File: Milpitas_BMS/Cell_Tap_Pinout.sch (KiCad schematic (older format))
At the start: 16 parts, among them J500 SOUTH CELL CONN, J501 NORTH CELL CONN

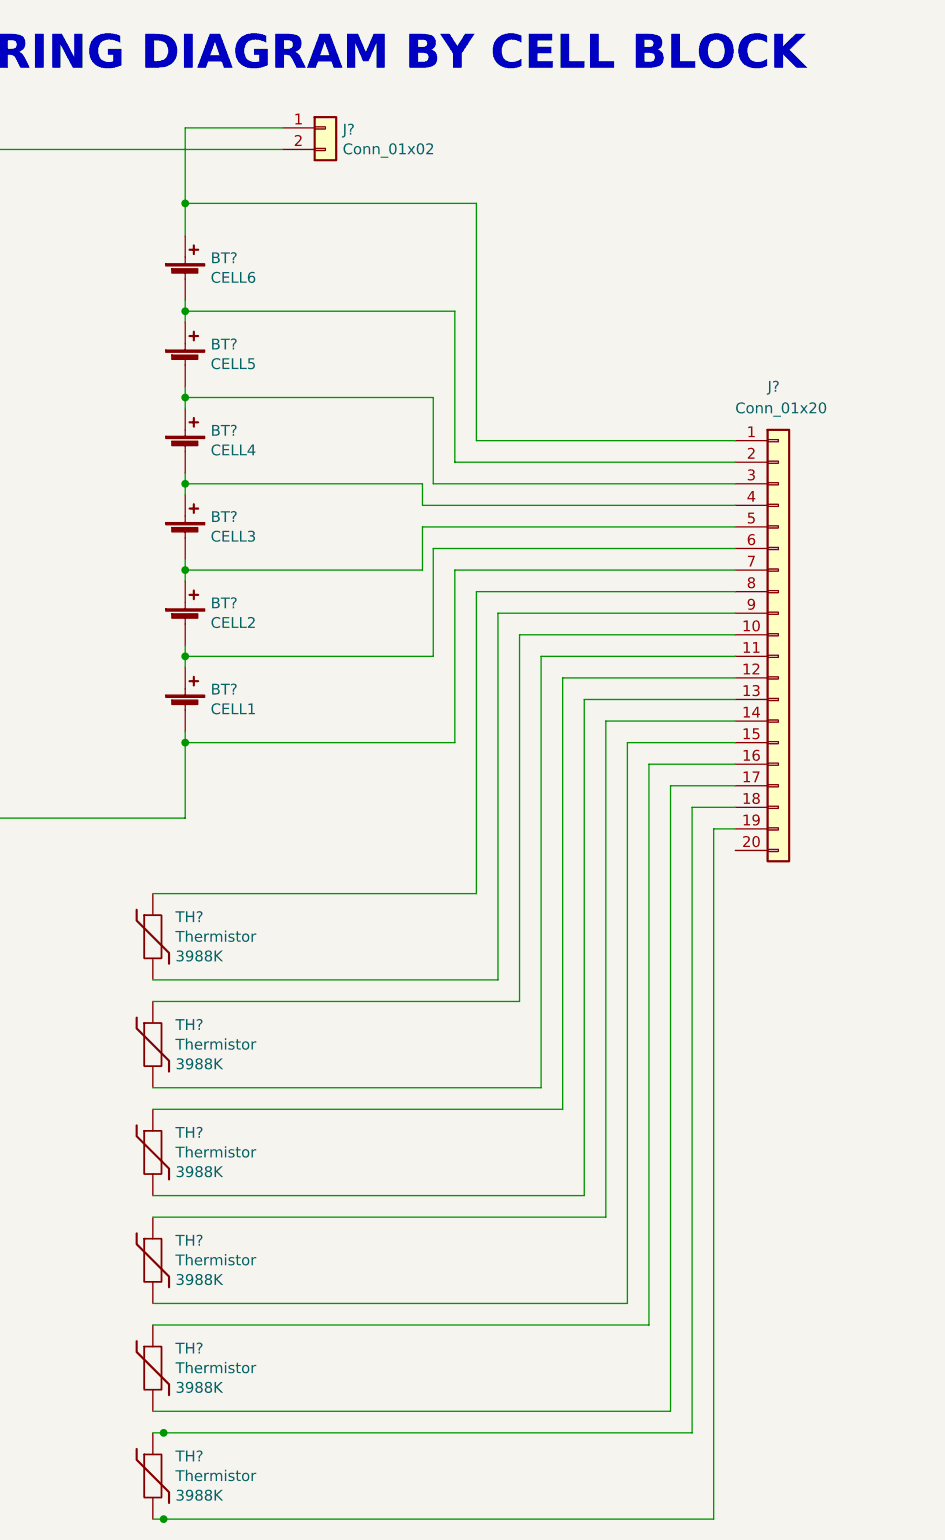
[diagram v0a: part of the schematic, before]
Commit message: updated some parts to inclued footprints + digikey P/N
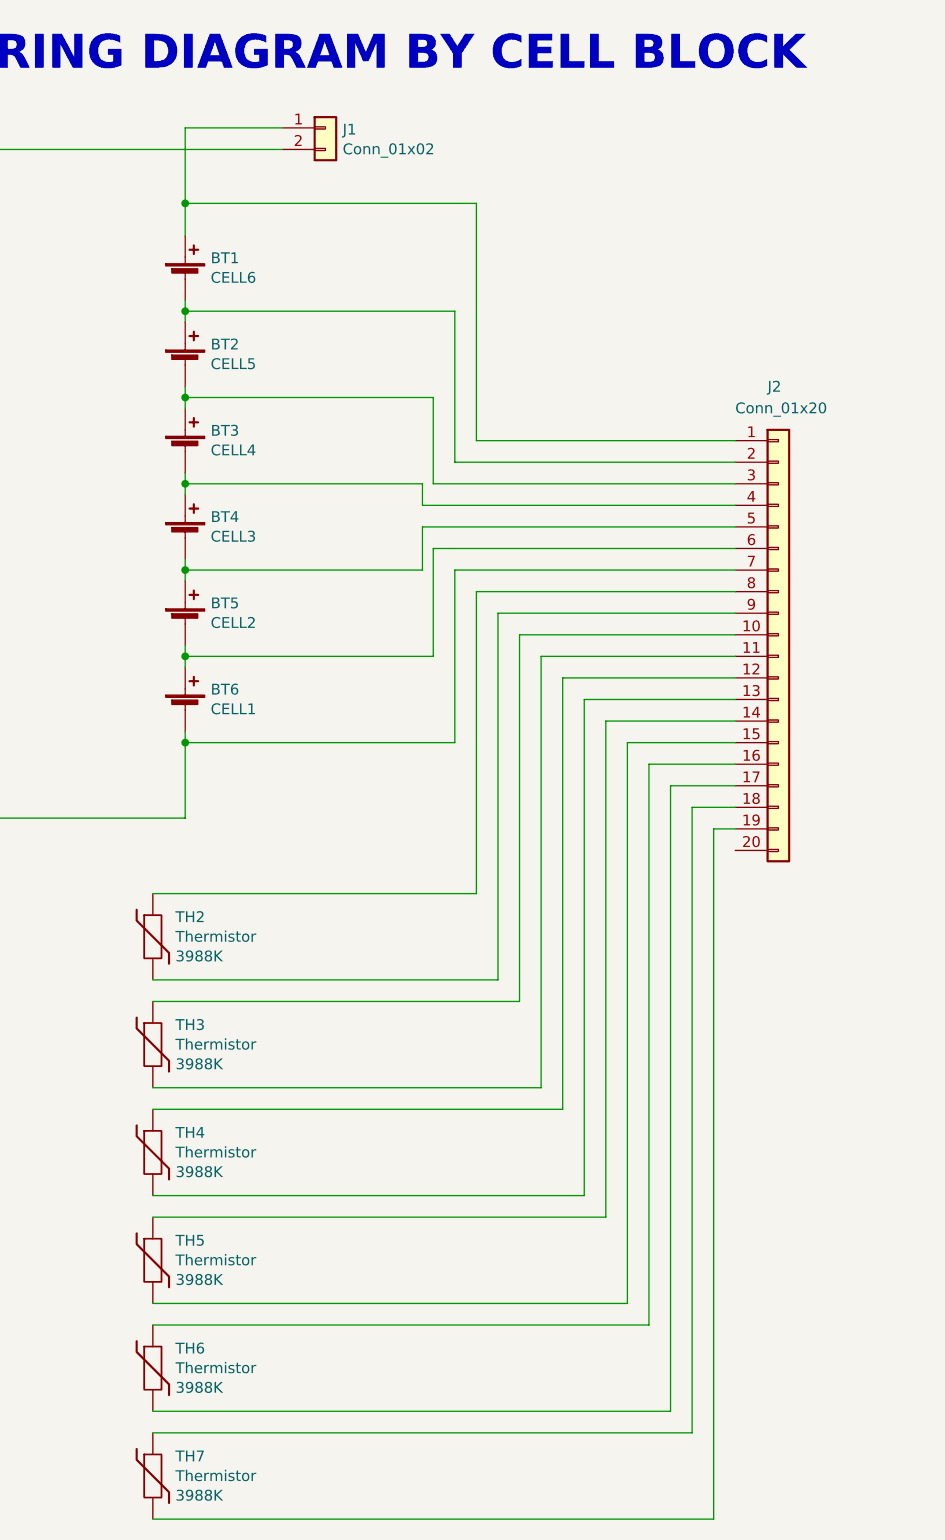
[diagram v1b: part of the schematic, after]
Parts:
- gave numbers to parts that had none: 14
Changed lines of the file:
@@
 AR Path="/62266D05" Ref="BT?"  Part="1"
 AR Path="/5FD4A06E/62266D05" Ref="BT?"  Part="1"
-AR Path="/5FD4A06E/62249708/62266D05" Ref="BT?"  Part="1"
-F 0 "BT?" H -3032 3396 50  0000 L CNN
+AR Path="/5FD4A06E/62249708/62266D05" Ref="BT6"  Part="1"
+F 0 "BT6" H -3032 3396 50  0000 L CNN
 F 1 "CELL1" H -3032 3305 50  0000 L CNN
 F 2 "" V -3150 3360 50  0001 C CNN
@@
 AR Path="/62266D0B" Ref="BT?"  Part="1"
 AR Path="/5FD4A06E/62266D0B" Ref="BT?"  Part="1"
-AR Path="/5FD4A06E/62249708/62266D0B" Ref="BT?"  Part="1"
-F 0 "BT?" H -3032 2996 50  0000 L CNN
+AR Path="/5FD4A06E/62249708/62266D0B" Ref="BT5"  Part="1"
+F 0 "BT5" H -3032 2996 50  0000 L CNN
 F 1 "CELL2" H -3032 2905 50  0000 L CNN
 F 2 "" V -3150 2960 50  0001 C CNN
@@
 AR Path="/62266D11" Ref="BT?"  Part="1"
 AR Path="/5FD4A06E/62266D11" Ref="BT?"  Part="1"
-AR Path="/5FD4A06E/62249708/62266D11" Ref="BT?"  Part="1"
-F 0 "BT?" H -3032 2596 50  0000 L CNN
+AR Path="/5FD4A06E/62249708/62266D11" Ref="BT4"  Part="1"
+F 0 "BT4" H -3032 2596 50  0000 L CNN
 F 1 "CELL3" H -3032 2505 50  0000 L CNN
 F 2 "" V -3150 2560 50  0001 C CNN
@@
 AR Path="/62266D17" Ref="BT?"  Part="1"
 AR Path="/5FD4A06E/62266D17" Ref="BT?"  Part="1"
-AR Path="/5FD4A06E/62249708/62266D17" Ref="BT?"  Part="1"
-F 0 "BT?" H -3032 2196 50  0000 L CNN
+AR Path="/5FD4A06E/62249708/62266D17" Ref="BT3"  Part="1"
+F 0 "BT3" H -3032 2196 50  0000 L CNN
 F 1 "CELL4" H -3032 2105 50  0000 L CNN
 F 2 "" V -3150 2160 50  0001 C CNN
@@
 AR Path="/62266D1D" Ref="BT?"  Part="1"
 AR Path="/5FD4A06E/62266D1D" Ref="BT?"  Part="1"
-AR Path="/5FD4A06E/62249708/62266D1D" Ref="BT?"  Part="1"
-F 0 "BT?" H -3032 1796 50  0000 L CNN
+AR Path="/5FD4A06E/62249708/62266D1D" Ref="BT2"  Part="1"
+F 0 "BT2" H -3032 1796 50  0000 L CNN
 F 1 "CELL5" H -3032 1705 50  0000 L CNN
 F 2 "" V -3150 1760 50  0001 C CNN
@@
 AR Path="/62266D23" Ref="BT?"  Part="1"
 AR Path="/5FD4A06E/62266D23" Ref="BT?"  Part="1"
-AR Path="/5FD4A06E/62249708/62266D23" Ref="BT?"  Part="1"
-F 0 "BT?" H -3032 1396 50  0000 L CNN
+AR Path="/5FD4A06E/62249708/62266D23" Ref="BT1"  Part="1"
+F 0 "BT1" H -3032 1396 50  0000 L CNN
 F 1 "CELL6" H -3032 1305 50  0000 L CNN
 F 2 "" V -3150 1360 50  0001 C CNN
@@
 AR Path="/62266D3F" Ref="J?"  Part="1"
 AR Path="/5FD4A06E/62266D3F" Ref="J?"  Part="1"
-AR Path="/5FD4A06E/62249708/62266D3F" Ref="J?"  Part="1"
-F 0 "J?" H -2420 592 50  0000 L CNN
+AR Path="/5FD4A06E/62249708/62266D3F" Ref="J1"  Part="1"
+F 0 "J1" H -2420 592 50  0000 L CNN
 F 1 "Conn_01x02" H -2420 501 50  0000 L CNN
 F 2 "" H -2500 600 50  0001 C CNN
@@
 AR Path="/62266D99" Ref="J?"  Part="1"
 AR Path="/5FD4A06E/62266D99" Ref="J?"  Part="1"
-AR Path="/5FD4A06E/62249708/62266D99" Ref="J?"  Part="1"
-F 0 "J?" H -450 4100 50  0000 L CNN
+AR Path="/5FD4A06E/62249708/62266D99" Ref="J2"  Part="1"
+F 0 "J2" H -450 4100 50  0000 L CNN
 F 1 "Conn_01x20" H -600 4000 50  0000 L CNN
 F 2 "" H -400 2950 50  0001 C CNN
@@
 	-800 3750 -600 3750
 Wire Wire Line
-	-3300 6650 -3250 6650
-Wire Wire Line
 	-700 7050 -700 3850
 Wire Wire Line
 	-700 3850 -600 3850
-Wire Wire Line
-	-3300 7050 -3250 7050
 Text Notes -4350 350  0    157  ~ 31
 WIRING DIAGRAM BY CELL BLOCK
@@
 AR Path="/5FBE719C/6336C00C" Ref="TH?"  Part="1"
 AR Path="/614D0E92/6336C00C" Ref="TH?"  Part="1"
-AR Path="/5FD4A06E/62249708/6336C00C" Ref="TH?"  Part="1"
-F 0 "TH?" H -3195 4441 50  0000 L CNN
+AR Path="/5FD4A06E/62249708/6336C00C" Ref="TH2"  Part="1"
+F 0 "TH2" H -3195 4441 50  0000 L CNN
 F 1 "Thermistor" H -3195 4350 50  0000 L CNN
 F 2 "" H -3300 4350 50  0001 C CNN
@@
 AR Path="/5FBE719C/63370CC6" Ref="TH?"  Part="1"
 AR Path="/614D0E92/63370CC6" Ref="TH?"  Part="1"
-AR Path="/5FD4A06E/62249708/63370CC6" Ref="TH?"  Part="1"
-F 0 "TH?" H -3195 4941 50  0000 L CNN
+AR Path="/5FD4A06E/62249708/63370CC6" Ref="TH3"  Part="1"
+F 0 "TH3" H -3195 4941 50  0000 L CNN
 F 1 "Thermistor" H -3195 4850 50  0000 L CNN
 F 2 "" H -3300 4850 50  0001 C CNN
@@
 AR Path="/5FBE719C/63375B6C" Ref="TH?"  Part="1"
 AR Path="/614D0E92/63375B6C" Ref="TH?"  Part="1"
-AR Path="/5FD4A06E/62249708/63375B6C" Ref="TH?"  Part="1"
-F 0 "TH?" H -3195 5441 50  0000 L CNN
+AR Path="/5FD4A06E/62249708/63375B6C" Ref="TH4"  Part="1"
+F 0 "TH4" H -3195 5441 50  0000 L CNN
 F 1 "Thermistor" H -3195 5350 50  0000 L CNN
 F 2 "" H -3300 5350 50  0001 C CNN
@@
 AR Path="/5FBE719C/6337AA60" Ref="TH?"  Part="1"
 AR Path="/614D0E92/6337AA60" Ref="TH?"  Part="1"
-AR Path="/5FD4A06E/62249708/6337AA60" Ref="TH?"  Part="1"
-F 0 "TH?" H -3195 5941 50  0000 L CNN
+AR Path="/5FD4A06E/62249708/6337AA60" Ref="TH5"  Part="1"
+F 0 "TH5" H -3195 5941 50  0000 L CNN
 F 1 "Thermistor" H -3195 5850 50  0000 L CNN
 F 2 "" H -3300 5850 50  0001 C CNN
@@
 AR Path="/5FBE719C/6337F900" Ref="TH?"  Part="1"
 AR Path="/614D0E92/6337F900" Ref="TH?"  Part="1"
-AR Path="/5FD4A06E/62249708/6337F900" Ref="TH?"  Part="1"
-F 0 "TH?" H -3195 6441 50  0000 L CNN
+AR Path="/5FD4A06E/62249708/6337F900" Ref="TH6"  Part="1"
+F 0 "TH6" H -3195 6441 50  0000 L CNN
 F 1 "Thermistor" H -3195 6350 50  0000 L CNN
 F 2 "" H -3300 6350 50  0001 C CNN
@@
 AR Path="/5FBE719C/63384764" Ref="TH?"  Part="1"
 AR Path="/614D0E92/63384764" Ref="TH?"  Part="1"
-AR Path="/5FD4A06E/62249708/63384764" Ref="TH?"  Part="1"
-F 0 "TH?" H -3195 6941 50  0000 L CNN
+AR Path="/5FD4A06E/62249708/63384764" Ref="TH7"  Part="1"
+F 0 "TH7" H -3195 6941 50  0000 L CNN
 F 1 "Thermistor" H -3195 6850 50  0000 L CNN
 F 2 "" H -3300 6850 50  0001 C CNN
@@
 	1    0    0    -1
 $EndComp
-Wire Bus Line
-	3250 4400 3250 6500
-Wire Bus Line
-	3200 1200 3200 3300
-Connection ~ -3250 6650
-Wire Wire Line
-	-3250 6650 -800 6650
-Connection ~ -3250 7050
-Wire Wire Line
-	-3250 7050 -700 7050
 $Bitmap
 Pos 9450 6850
@@
 EndData
 $EndBitmap
+Wire Wire Line
+	-3300 6650 -800 6650
+Wire Wire Line
+	-3300 7050 -700 7050
+Wire Bus Line
+	3250 4400 3250 6500
+Wire Bus Line
+	3200 1200 3200 3300
 $EndSCHEMATC

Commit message: lots of little fixes
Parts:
- J500, J501: footprint (none) -> Connector_Molex:Molex_Micro-Fit_3.0_43045-2000_2x10_P3.00mm_Horizontal; Digikey WM12752-ND -> WM4726-ND
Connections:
- net NORTH_CELL5 is gone; now on net NORTH_CELL_5: J501.2 (Pin_2)
- net SOUTH_CELL1 is gone; now on net SOUTH_CELL_1: J500.6 (Pin_6)
- net SOUTH_CELL5 is gone; now on net SOUTH_CELL_5: J500.2 (Pin_2)
- net NORTH_CELL0 renamed NORTH_CELL_0
- net NORTH_CELL1 renamed SOUTH_CELL_1
- net NORTH_CELL2 renamed NORTH_CELL_2
- net NORTH_CELL3 renamed NORTH_CELL_3
- net NORTH_CELL4 renamed NORTH_CELL_5
- net NORTH_CELL6 renamed NORTH_CELL_6
- net SOUTH_CELL0 renamed SOUTH_CELL_0
- net SOUTH_CELL2 renamed SOUTH_CELL_2
- net SOUTH_CELL3 renamed SOUTH_CELL_3
- net SOUTH_CELL4 renamed SOUTH_CELL_5
- net SOUTH_CELL6 renamed SOUTH_CELL_6

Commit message: prelim layout ???
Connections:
- net labels added: SOUTH_CELL_4
- net labels removed: A1, A10, A11, A12, A13, A14, A15, A16, A17, A18, A19, A2, A3, A4, A5, A6, A7, A8, A9
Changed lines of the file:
@@
 Wire Wire Line
 	2450 4300 3150 4300
-Text Label 3100 2900 2    39   ~ 0
+Text Label 5100 2750 2    39   ~ 0
 SOUTH_THERM6_N
-Text Label 3100 2800 2    39   ~ 0
+Text Label 5100 2650 2    39   ~ 0
 SOUTH_THERM6_P
 Wire Wire Line
-	2400 2900 3100 2900
-Wire Wire Line
-	2400 2800 3100 2800
-Text Label 3100 2700 2    39   ~ 0
+	4400 2750 5100 2750
+Wire Wire Line
+	4400 2650 5100 2650
+Text Label 5100 2550 2    39   ~ 0
 SOUTH_THERM5_N
-Text Label 3100 2600 2    39   ~ 0
+Text Label 5100 2450 2    39   ~ 0
 SOUTH_THERM5_P
 Wire Wire Line
-	2400 2700 3100 2700
-Wire Wire Line
-	2400 2600 3100 2600
-Text Label 3100 2500 2    39   ~ 0
+	4400 2550 5100 2550
+Wire Wire Line
+	4400 2450 5100 2450
+Text Label 5100 2350 2    39   ~ 0
 SOUTH_THERM4_N
-Text Label 3100 2400 2    39   ~ 0
+Text Label 5100 2250 2    39   ~ 0
 SOUTH_THERM4_P
 Wire Wire Line
-	2400 2500 3100 2500
-Wire Wire Line
-	2400 2400 3100 2400
-Text Label 3100 2300 2    39   ~ 0
+	4400 2350 5100 2350
+Wire Wire Line
+	4400 2250 5100 2250
+Text Label 5100 2150 2    39   ~ 0
 SOUTH_THERM3_N
-Text Label 3100 2200 2    39   ~ 0
+Text Label 5100 2050 2    39   ~ 0
 SOUTH_THERM3_P
 Wire Wire Line
-	2400 2300 3100 2300
-Wire Wire Line
-	2400 2200 3100 2200
-Text Label 3100 2100 2    39   ~ 0
+	4400 2150 5100 2150
+Wire Wire Line
+	4400 2050 5100 2050
+Text Label 5100 1950 2    39   ~ 0
 SOUTH_THERM2_N
-Text Label 3100 2000 2    39   ~ 0
+Text Label 5100 1850 2    39   ~ 0
 SOUTH_THERM2_P
 Wire Wire Line
-	2400 2100 3100 2100
-Wire Wire Line
-	2400 2000 3100 2000
-Text Label 3100 1900 2    39   ~ 0
+	4400 1950 5100 1950
+Wire Wire Line
+	4400 1850 5100 1850
+Text Label 5100 1750 2    39   ~ 0
 SOUTH_THERM1_N
-Text Label 3100 1800 2    39   ~ 0
+Text Label 5100 1650 2    39   ~ 0
 SOUTH_THERM1_P
 Wire Wire Line
-	2400 1900 3100 1900
-Wire Wire Line
-	2400 1800 3100 1800
+	4400 1750 5100 1750
+Wire Wire Line
+	4400 1650 5100 1650
 $Comp
 L Connector_Generic:Conn_01x20 J?
@@
 	-1   0    0    -1
 $EndComp
-Text Label 3100 1100 2    39   ~ 0
+Text Label 3100 2800 2    39   ~ 0
 SOUTH_CELL6
-Text Label 3100 1200 2    39   ~ 0
+Text Label 3100 2700 2    39   ~ 0
 SOUTH_CELL5
-Text Label 3100 1300 2    39   ~ 0
+Text Label 3100 2600 2    39   ~ 0
 SOUTH_CELL4
-Text Label 3100 1400 2    39   ~ 0
+Text Label 3100 2500 2    39   ~ 0
 SOUTH_CELL3
-Text Label 3100 1500 2    39   ~ 0
+Text Label 3100 2400 2    39   ~ 0
 SOUTH_CELL2
-Text Label 3100 1600 2    39   ~ 0
+Text Label 3100 2300 2    39   ~ 0
 SOUTH_CELL1
-Text Label 3100 1700 2    39   ~ 0
+Text Label 3100 2200 2    39   ~ 0
 SOUTH_CELL0
 Wire Wire Line
-	2400 1700 3100 1700
-Wire Wire Line
-	2400 1600 3100 1600
-Wire Wire Line
-	2400 1500 3100 1500
-Wire Wire Line
-	2400 1400 3100 1400
-Wire Wire Line
-	2400 1300 3100 1300
-Wire Wire Line
-	2400 1200 3100 1200
-Wire Wire Line
-	2400 1100 3100 1100
+	2400 2200 3100 2200
+Wire Wire Line
+	2400 2300 3100 2300
+Wire Wire Line
+	2400 2400 3100 2400
+Wire Wire Line
+	2400 2500 3100 2500
+Wire Wire Line
+	2400 2600 3100 2600
+Wire Wire Line
+	2400 2700 3100 2700
+Wire Wire Line
+	2400 2800 3100 2800
 $Comp
 L Device:Battery_Cell BT?
@@
 Wire Wire Line
 	-3300 7050 -700 7050
-Text Label 2400 1100 0    39   ~ 0
-A1
-Text Label 2400 1200 0    39   ~ 0
-A2
-Text Label 2400 1300 0    39   ~ 0
-A3
-Text Label 2400 1400 0    39   ~ 0
-A4
-Text Label 2400 1500 0    39   ~ 0
-A5
-Text Label 2400 1600 0    39   ~ 0
-A6
-Text Label 2400 1700 0    39   ~ 0
-A7
-Text Label 2400 1800 0    39   ~ 0
-A8
-Text Label 2400 1900 0    39   ~ 0
-A9
-Text Label 2400 2000 0    39   ~ 0
-A10
-Text Label 2400 2100 0    39   ~ 0
-A11
-Text Label 2400 2200 0    39   ~ 0
-A12
-Text Label 2400 2300 0    39   ~ 0
-A13
-Text Label 2400 2400 0    39   ~ 0
-A14
-Text Label 2400 2500 0    39   ~ 0
-A15
-Text Label 2400 2600 0    39   ~ 0
-A16
-Text Label 2400 2700 0    39   ~ 0
-A17
-Text Label 2400 2800 0    39   ~ 0
-A18
-Text Label 2400 2900 0    39   ~ 0
-A19
-Text GLabel 3100 1100 2    39   Input ~ 0
+Text GLabel 3100 2800 2    39   Input ~ 0
 SOUTH_CELL_6
-Text GLabel 3100 1200 2    39   Input ~ 0
+Text GLabel 3100 2700 2    39   Input ~ 0
 SOUTH_CELL_5
-Text GLabel 3100 1300 2    39   Input ~ 0
-SOUTH_CELL_5
-Text GLabel 3100 1400 2    39   Input ~ 0
+Text GLabel 3100 2600 2    39   Input ~ 0
+SOUTH_CELL_4
+Text GLabel 3100 2500 2    39   Input ~ 0
 SOUTH_CELL_3
-Text GLabel 3100 1500 2    39   Input ~ 0
+Text GLabel 3100 2400 2    39   Input ~ 0
 SOUTH_CELL_2
-Text GLabel 3100 1600 2    39   Input ~ 0
+Text GLabel 3100 2300 2    39   Input ~ 0
 SOUTH_CELL_1
-Text GLabel 3100 1700 2    39   Input ~ 0
+Text GLabel 3100 2200 2    39   Input ~ 0
 SOUTH_CELL_0
-Text GLabel 3100 1800 2    39   Input ~ 0
+Text GLabel 5100 1650 2    39   Input ~ 0
 SOUTH_THERM1_P
-Text GLabel 3100 1900 2    39   Input ~ 0
+Text GLabel 5100 1750 2    39   Input ~ 0
 SOUTH_THERM1_N
-Text GLabel 3100 2000 2    39   Input ~ 0
+Text GLabel 5100 1850 2    39   Input ~ 0
 SOUTH_THERM2_P
-Text GLabel 3100 2200 2    39   Input ~ 0
+Text GLabel 5100 2050 2    39   Input ~ 0
 SOUTH_THERM3_P
-Text GLabel 3100 2300 2    39   Input ~ 0
+Text GLabel 5100 2150 2    39   Input ~ 0
 SOUTH_THERM3_N
-Text GLabel 3100 2400 2    39   Input ~ 0
+Text GLabel 5100 2250 2    39   Input ~ 0
 SOUTH_THERM4_P
-Text GLabel 3100 2500 2    39   Input ~ 0
+Text GLabel 5100 2350 2    39   Input ~ 0
 SOUTH_THERM4_N
-Text GLabel 3100 2600 2    39   Input ~ 0
+Text GLabel 5100 2450 2    39   Input ~ 0
 SOUTH_THERM5_P
-Text GLabel 3100 2700 2    39   Input ~ 0
+Text GLabel 5100 2550 2    39   Input ~ 0
 SOUTH_THERM5_N
-Text GLabel 3100 2800 2    39   Input ~ 0
+Text GLabel 5100 2650 2    39   Input ~ 0
 SOUTH_THERM6_P
-Text GLabel 3100 2900 2    39   Input ~ 0
+Text GLabel 5100 2750 2    39   Input ~ 0
 SOUTH_THERM6_N
-Text GLabel 3100 2100 2    39   Input ~ 0
+Text GLabel 5100 1950 2    39   Input ~ 0
 SOUTH_THERM2_N
 Text GLabel 3150 4300 2    39   Input ~ 0
